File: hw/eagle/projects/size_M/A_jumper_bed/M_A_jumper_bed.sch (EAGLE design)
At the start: 17 parts

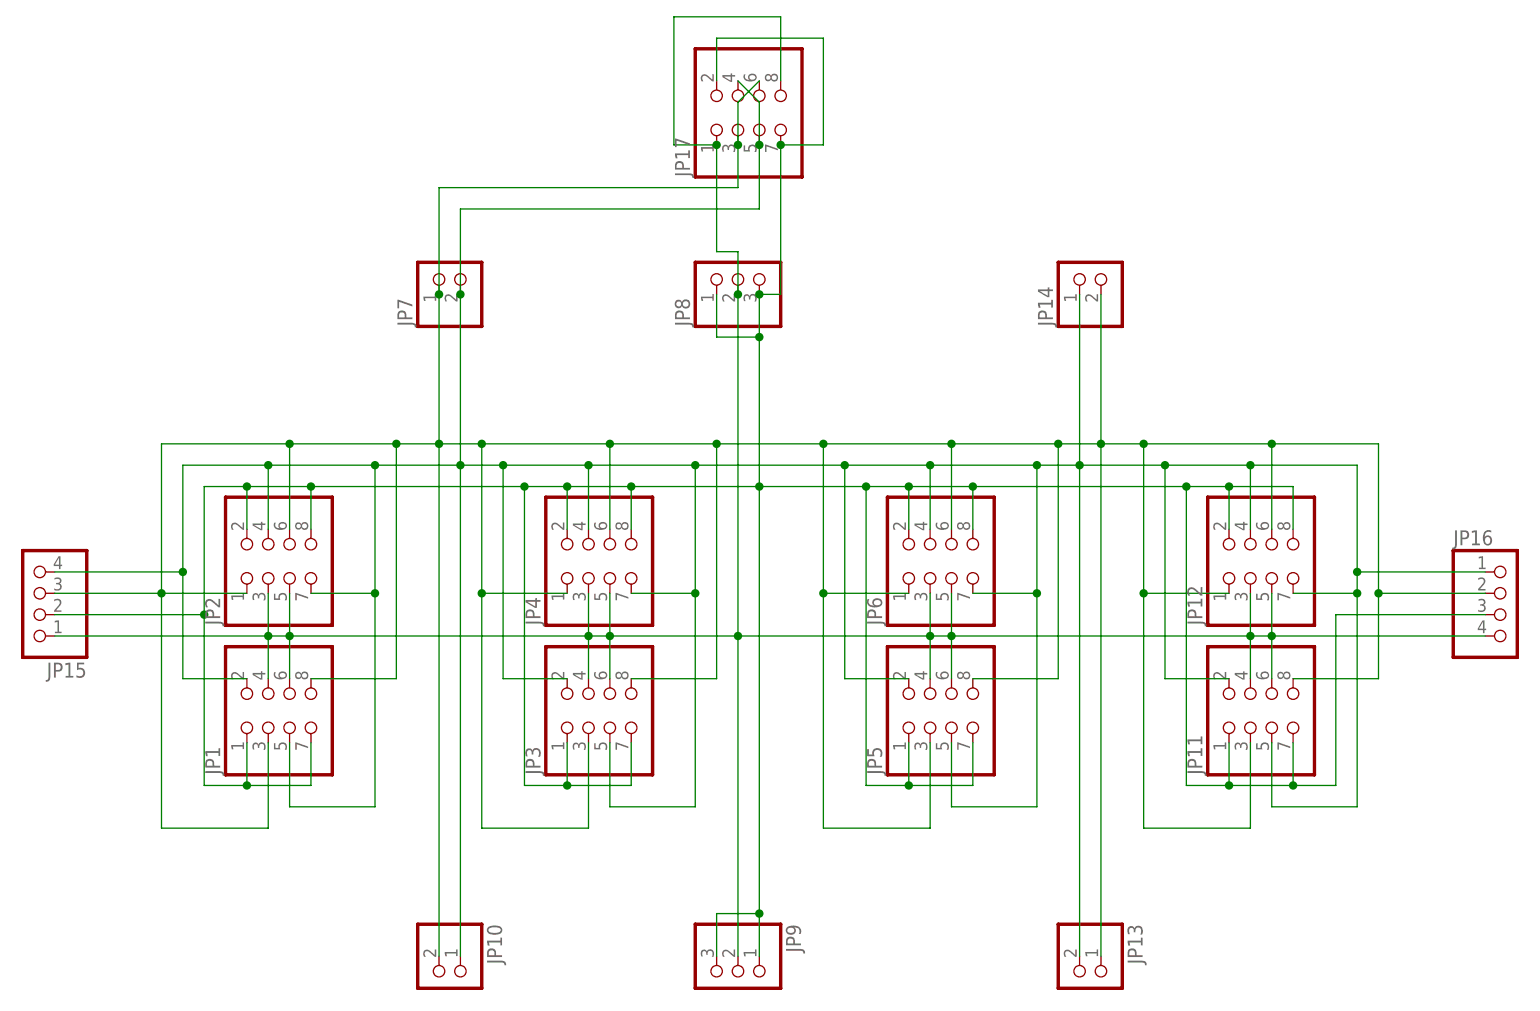
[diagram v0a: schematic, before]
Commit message: PCB subfolder restructured to the type_id_letter_name format
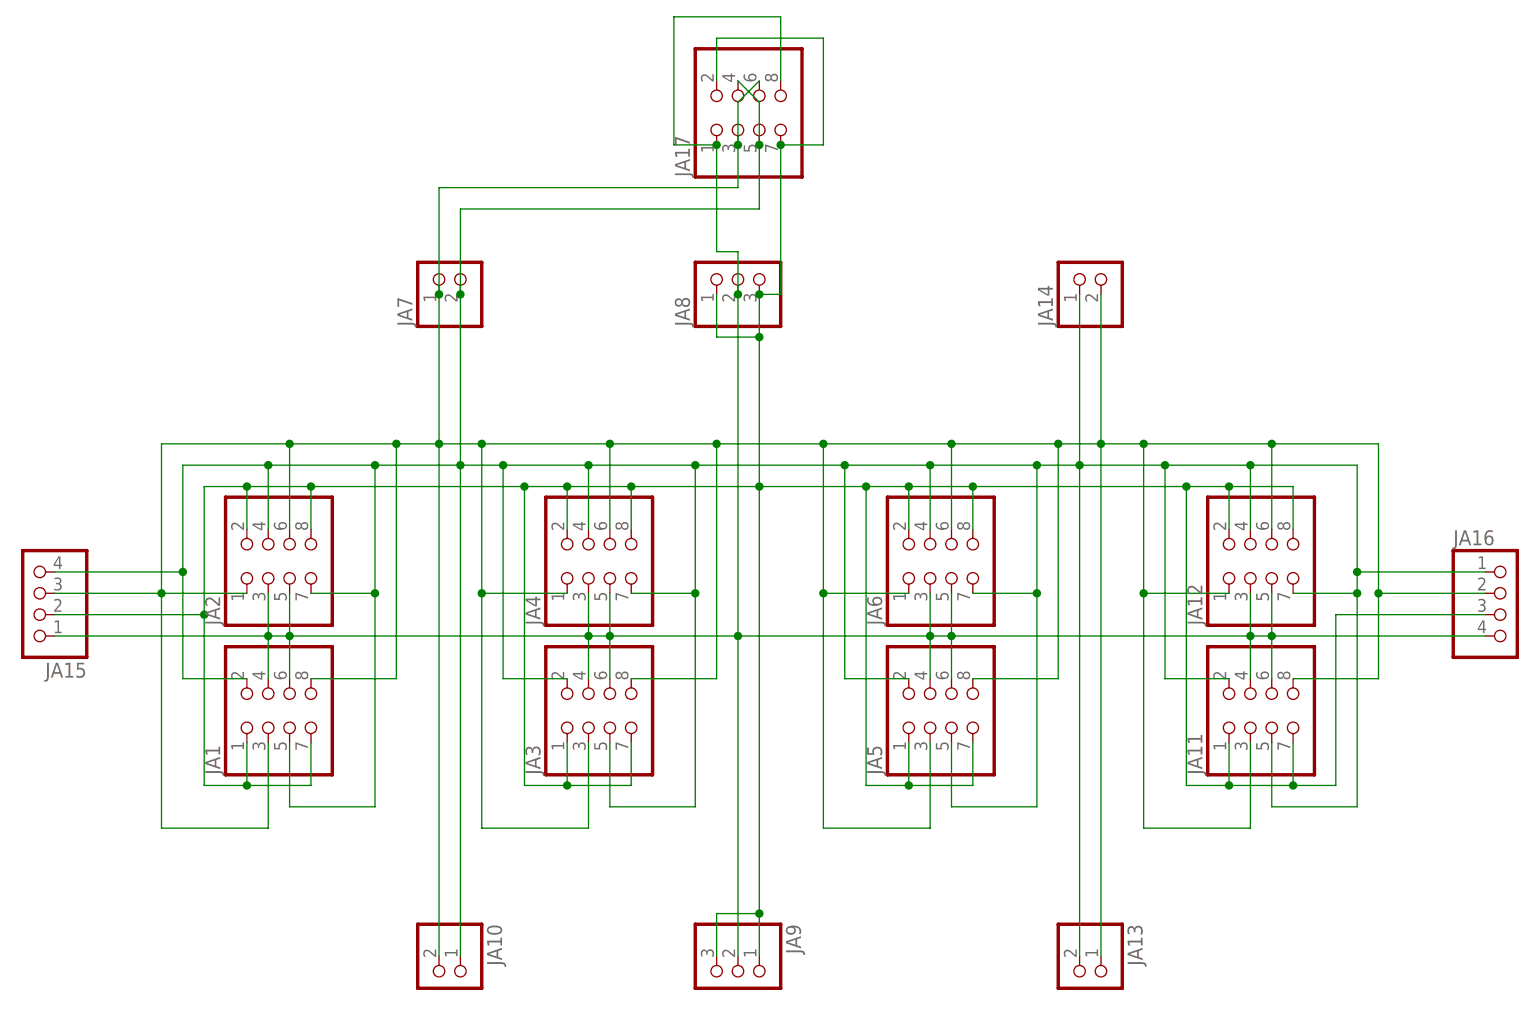
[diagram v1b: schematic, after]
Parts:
- renumbered JP1 to JA1, JP10 to JA10, JP11 to JA11, JP12 to JA12, JP13 to JA13, JP14 to JA14, JP15 to JA15, JP16 to JA16, JP17 to JA17, JP2 to JA2, JP3 to JA3, JP4 to JA4, JP5 to JA5, JP6 to JA6, JP7 to JA7, JP8 to JA8, JP9 to JA9

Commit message: pcb M.1 -not finished
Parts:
- removed JA17: (no value), pinhead2:PINHD-2X4/90
- renumbered JA1 to A.J1, JA10 to A.J10, JA11 to A.J11, JA12 to A.J12, JA13 to A.J13, JA14 to A.J14, JA15 to A.J15, JA16 to A.J16, JA2 to A.J2, JA3 to A.J3, JA4 to A.J4, JA5 to A.J5, JA6 to A.J6, JA7 to A.J7, JA8 to A.J8, JA9 to A.J9
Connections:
- net GND: no longer JA17.2, JA17.7
- net SCL: no longer JA17.4, JA17.5
- net SDA: no longer JA17.3, JA17.6
- net VCC: no longer JA17.1, JA17.8
